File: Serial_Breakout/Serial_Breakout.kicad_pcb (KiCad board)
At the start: 2 copper layers, 56.4 x 23.8 mm, 3 parts, among them J1 VIC Serial In, J2 Disc Serial Out, J3 Breakout

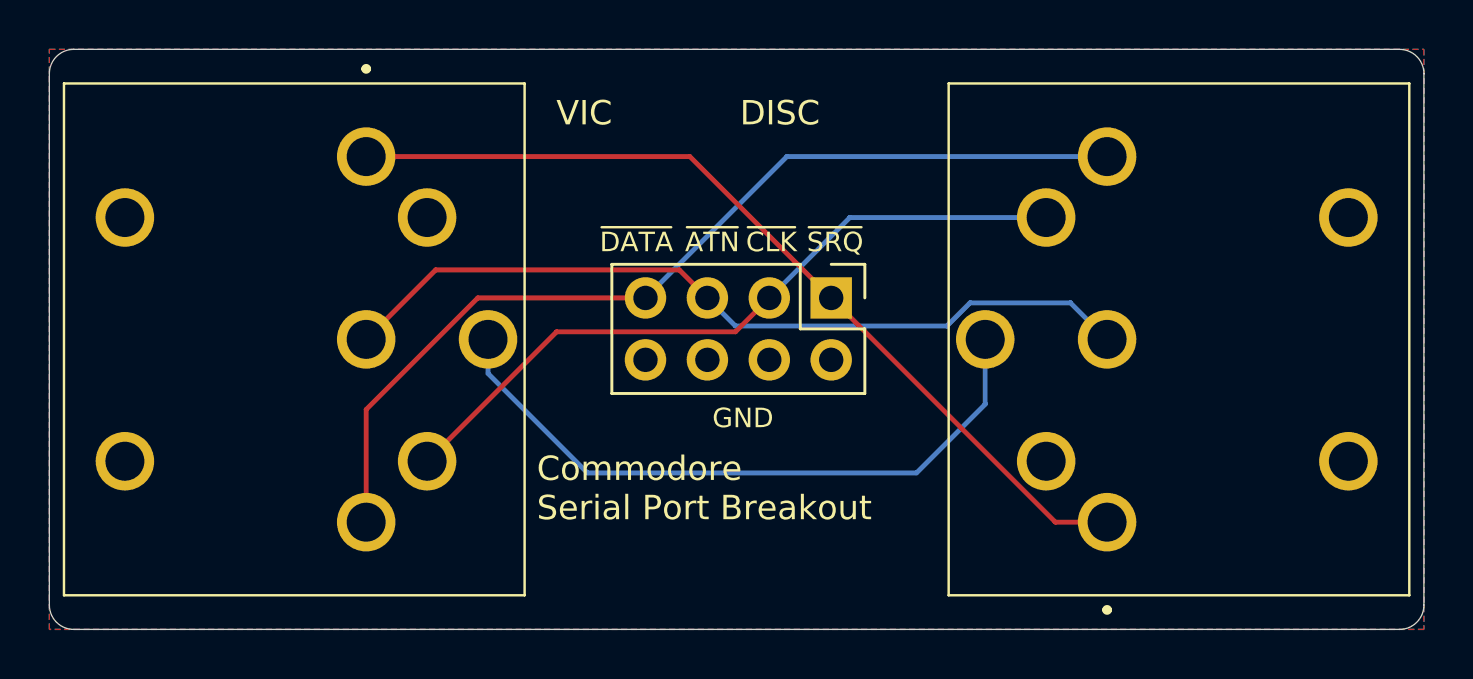
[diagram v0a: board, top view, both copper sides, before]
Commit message: Cleaning up designs
Keeping just the DIN-to-DIN breakout
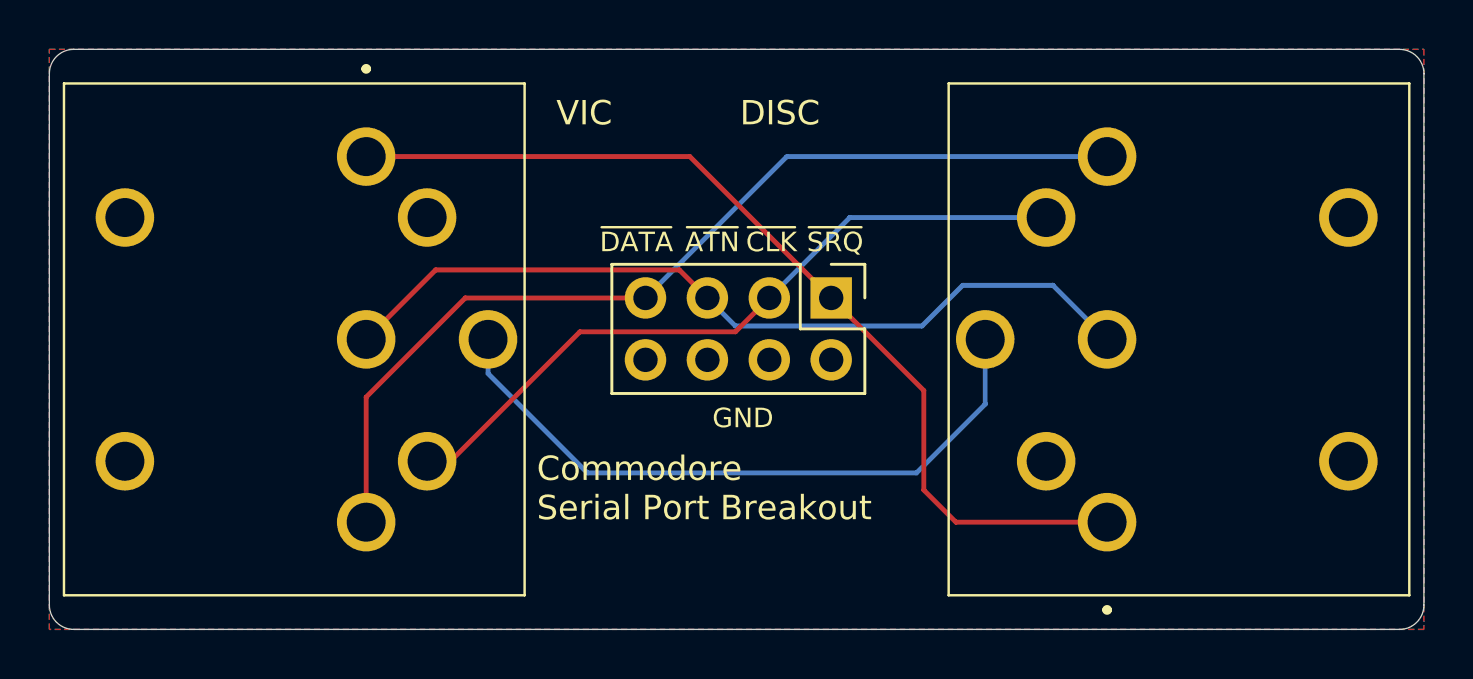
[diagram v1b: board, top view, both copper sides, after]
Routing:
- net /~{SRQIN}: track 36.6 -> 39.0 mm
- net /~{ATN}: track 33.6 -> 34.1 mm
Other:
- board text added: "Brett Hallen, Feb 2026 www.youtube.com/@Brfff"
- board text removed: "Brett Hallen, Nov 2025 www.youtube.com/@Brfff"
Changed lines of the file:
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@@
 		)
 	)
-	(gr_text "Brett Hallen, Nov 2025\nwww.youtube.com/@Brfff"
+	(gr_text "Brett Hallen, Feb 2026\nwww.youtube.com/@Brfff"
 		(at 107.08 64.08 0)
 		(layer "B.SilkS")
@@
 	)
 	(segment
-		(start 82.5 73.477265)
-		(end 87.077265 68.9)
+		(start 82.5 72.968632)
+		(end 86.568632 68.9)
 		(width 0.2)
 		(layer "F.Cu")
@@
 	(segment
 		(start 82.5 78.1)
-		(end 82.5 73.477265)
+		(end 82.5 72.968632)
 		(width 0.2)
 		(layer "F.Cu")
@@
 	)
 	(segment
-		(start 87.077265 68.9)
+		(start 86.568632 68.9)
 		(end 93.96 68.9)
 		(width 0.2)
@@
 	)
 	(segment
-		(start 111.399 69.099)
+		(start 97.651 70.051)
+		(end 105.309 70.051)
+		(width 0.2)
+		(layer "B.Cu")
+		(net 3)
+	)
+	(segment
+		(start 110.68 68.38)
 		(end 112.9 70.6)
 		(width 0.2)
@@
 	)
 	(segment
-		(start 97.651 70.051)
-		(end 106.326265 70.051)
-		(width 0.2)
-		(layer "B.Cu")
-		(net 3)
-	)
-	(segment
-		(start 107.278265 69.099)
-		(end 111.399 69.099)
-		(width 0.2)
-		(layer "B.Cu")
-		(net 3)
-	)
-	(segment
-		(start 106.326265 70.051)
-		(end 107.278265 69.099)
+		(start 105.309 70.051)
+		(end 106.98 68.38)
 		(width 0.2)
 		(layer "B.Cu")
@@
 	)
 	(segment
-		(start 82.5 63.1)
-		(end 95.78 63.1)
+		(start 106.98 68.38)
+		(end 110.68 68.38)
+		(width 0.2)
+		(layer "B.Cu")
+		(net 3)
+	)
+	(segment
+		(start 101.58 68.9)
+		(end 105.38 72.7)
 		(width 0.2)
 		(layer "F.Cu")
@@
 	)
 	(segment
-		(start 101.58 68.902735)
-		(end 110.777265 78.1)
+		(start 82.5 63.1)
+		(end 95.78 63.1)
 		(width 0.2)
 		(layer "F.Cu")
@@
 	)
 	(segment
-		(start 101.58 68.9)
-		(end 101.58 68.902735)
+		(start 105.38 72.7)
+		(end 105.38 76.78)
 		(width 0.2)
 		(layer "F.Cu")
@@
 	)
 	(segment
-		(start 110.777265 78.1)
+		(start 106.7 78.1)
 		(end 112.9 78.1)
+		(width 0.2)
+		(layer "F.Cu")
+		(net 4)
+	)
+	(segment
+		(start 105.38 76.78)
+		(end 106.7 78.1)
 		(width 0.2)
 		(layer "F.Cu")
@@
 	(segment
 		(start 85 75.6)
-		(end 90.311 70.289)
+		(end 85.96 75.6)
 		(width 0.2)
 		(layer "F.Cu")
@@
 	)
 	(segment
-		(start 90.311 70.289)
+		(start 85.96 75.6)
+		(end 91.271 70.289)
+		(width 0.2)
+		(layer "F.Cu")
+		(net 5)
+	)
+	(segment
+		(start 91.271 70.289)
 		(end 97.651 70.289)
 		(width 0.2)
